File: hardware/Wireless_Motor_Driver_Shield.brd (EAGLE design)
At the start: 59.7 x 53.3 mm, 97 parts, among them J1 5.5x2.1mm Barrel, Q1 MOSFET-NCHANNELBSS138, Q2 MOSFET-NCHANNELBSS138, Q3 MMBT2222A, Q4 DMG2307L, Q5 DMG2307L, Q6 DMG2307L, U1 XBEE-1XBEE-1_LOCK, U2 ARDUINO, U3 TB6612FNG

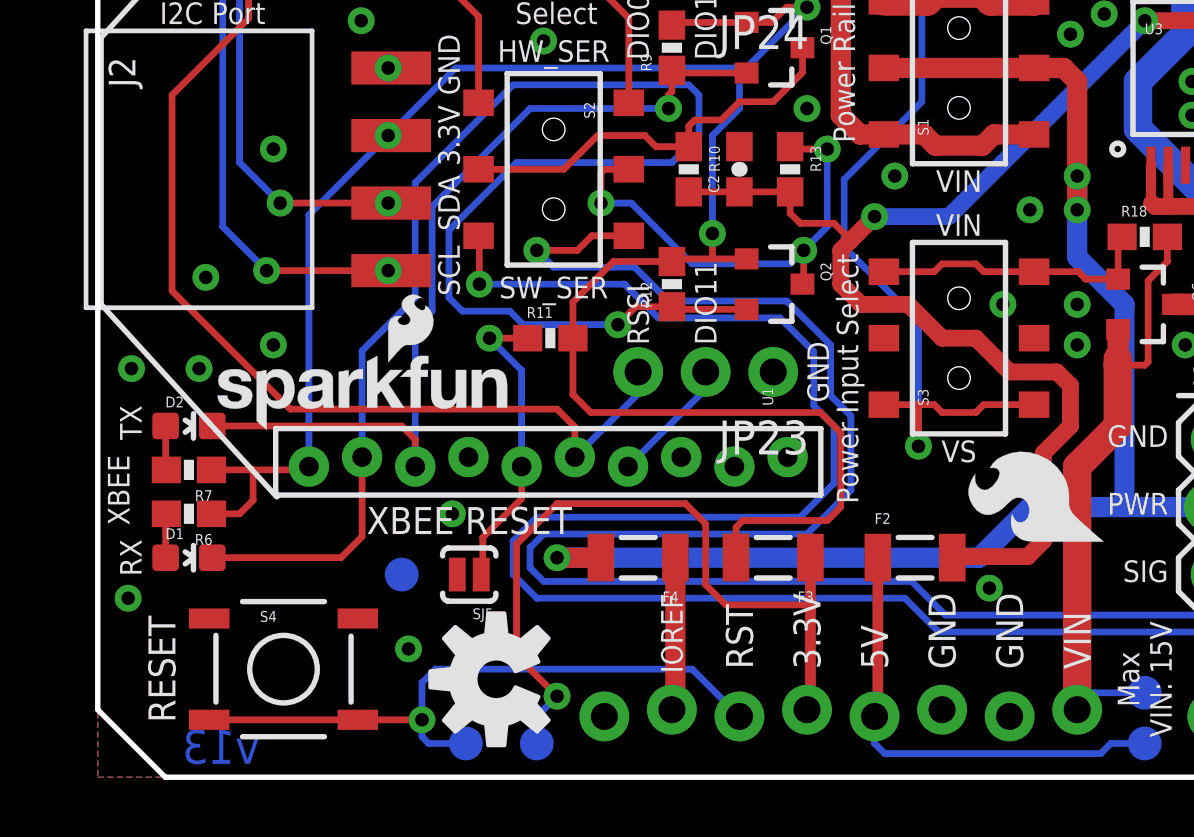
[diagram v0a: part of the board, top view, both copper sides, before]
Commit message: Changed to v14. Changed switch labels to VMOTOR
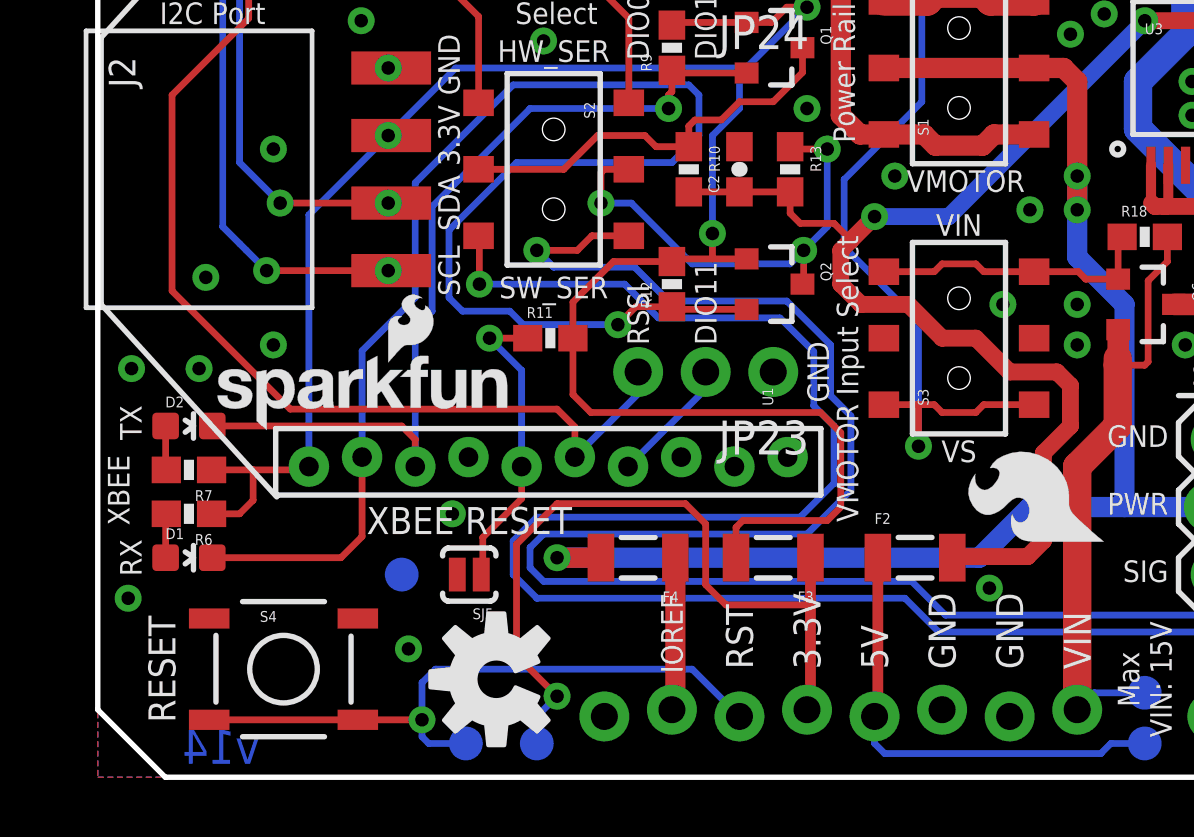
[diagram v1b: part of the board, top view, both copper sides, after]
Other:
- board text added: "VMOTOR"
- board text added: "VMOTOR Input Select"
- board text added: "v14"
- board text removed: "Power Input Select"
- board text removed: "v13"
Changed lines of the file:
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@@
 <grid distance="0.01" unitdist="inch" unit="inch" style="dots" multiple="1" display="yes" altdistance="0.005" altunitdist="inch" altunit="inch"/>
 <layers>
-<layer number="1" name="Top" color="4" fill="1" visible="no" active="yes"/>
+<layer number="1" name="Top" color="4" fill="1" visible="yes" active="yes"/>
 <layer number="2" name="Route2" color="1" fill="3" visible="no" active="yes"/>
 <layer number="15" name="Route15" color="4" fill="6" visible="no" active="yes"/>
-<layer number="16" name="Bottom" color="1" fill="1" visible="yes" active="yes"/>
+<layer number="16" name="Bottom" color="1" fill="1" visible="no" active="yes"/>
 <layer number="17" name="Pads" color="2" fill="1" visible="yes" active="yes"/>
 <layer number="18" name="Vias" color="2" fill="1" visible="yes" active="yes"/>
 <layer number="19" name="Unrouted" color="6" fill="1" visible="yes" active="yes"/>
 <layer number="20" name="Dimension" color="15" fill="1" visible="yes" active="yes"/>
-<layer number="21" name="tPlace" color="16" fill="1" visible="no" active="yes"/>
-<layer number="22" name="bPlace" color="14" fill="1" visible="yes" active="yes"/>
-<layer number="23" name="tOrigins" color="15" fill="1" visible="no" active="yes"/>
-<layer number="24" name="bOrigins" color="15" fill="1" visible="yes" active="yes"/>
+<layer number="21" name="tPlace" color="16" fill="1" visible="yes" active="yes"/>
+<layer number="22" name="bPlace" color="14" fill="1" visible="no" active="yes"/>
+<layer number="23" name="tOrigins" color="15" fill="1" visible="yes" active="yes"/>
+<layer number="24" name="bOrigins" color="15" fill="1" visible="no" active="yes"/>
 <layer number="25" name="tNames" color="7" fill="1" visible="no" active="yes"/>
 <layer number="26" name="bNames" color="7" fill="1" visible="no" active="yes"/>
@@
 <text x="40.259" y="10.287" size="0.8128" layer="21" font="vector" ratio="15" align="center-right">PWR</text>
 <text x="40.259" y="7.747" size="0.8128" layer="21" font="vector" ratio="15" align="center-right">SIG</text>
-<text x="6.096" y="0.508" size="1.27" layer="16" font="vector" ratio="15" rot="SMR0">v13</text>
+<text x="6.096" y="0.508" size="1.27" layer="16" font="vector" ratio="15" rot="SMR0">v14</text>
 <text x="27.94" y="-10.16" size="1.778" layer="51" font="vector" ratio="10">B. Huang</text>
 <text x="12.7" y="49.657" size="0.8128" layer="21" ratio="15" rot="R270" align="center-left">SDA</text>
@@
 <wire x1="48.514" y1="31.75" x2="48.514" y2="21.59" width="0.2032" layer="21"/>
 <wire x1="48.514" y1="21.59" x2="51.054" y2="21.59" width="0.2032" layer="21"/>
-<text x="32.385" y="22.8219" size="0.8128" layer="21" font="vector" ratio="15" rot="R180" align="bottom-center">VIN</text>
+<text x="32.639" y="22.8219" size="0.8128" layer="21" font="vector" ratio="15" rot="R180" align="bottom-center">VMOTOR</text>
 <text x="32.385" y="30.5054" size="0.8128" layer="21" font="vector" ratio="15" rot="R180" align="top-center">IOREF</text>
 <dimension x1="59.69" y1="0" x2="55.88" y2="53.34" x3="67.31" y3="26.67" textsize="1.778" textratio="15" layer="47" dtype="vertical" unit="inch"/>
@@
 <text x="5.08" y="50.165" size="0.8128" layer="21" font="vector" ratio="15" rot="R90" align="center">Max
 VS: 15V</text>
-<text x="28.194" y="14.986" size="0.8128" layer="21" font="vector" ratio="15" rot="R90" align="center">Power Input Select</text>
+<text x="28.194" y="14.986" size="0.8128" layer="21" font="vector" ratio="15" rot="R90" align="center">VMOTOR Input Select</text>
 <text x="0.635" y="24.13" size="0.8128" layer="22" font="vector" ratio="15" rot="MR180" align="center-left">3.3V</text>
 <text x="0.635" y="26.67" size="0.8128" layer="22" font="vector" ratio="15" rot="MR180" align="center-left">GND</text>
